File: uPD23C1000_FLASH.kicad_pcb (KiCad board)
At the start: 2 copper layers, 16.4 x 34.2 mm, 7 parts, among them J1 uPD23C1000, J2 Conn_1x2, J3 Conn_1x3, U1 GLS29EE010 (TSOP), U2 SST39SF010 (TSOP), U3 SST39SF010 / GLS29EE010 (PLCC)

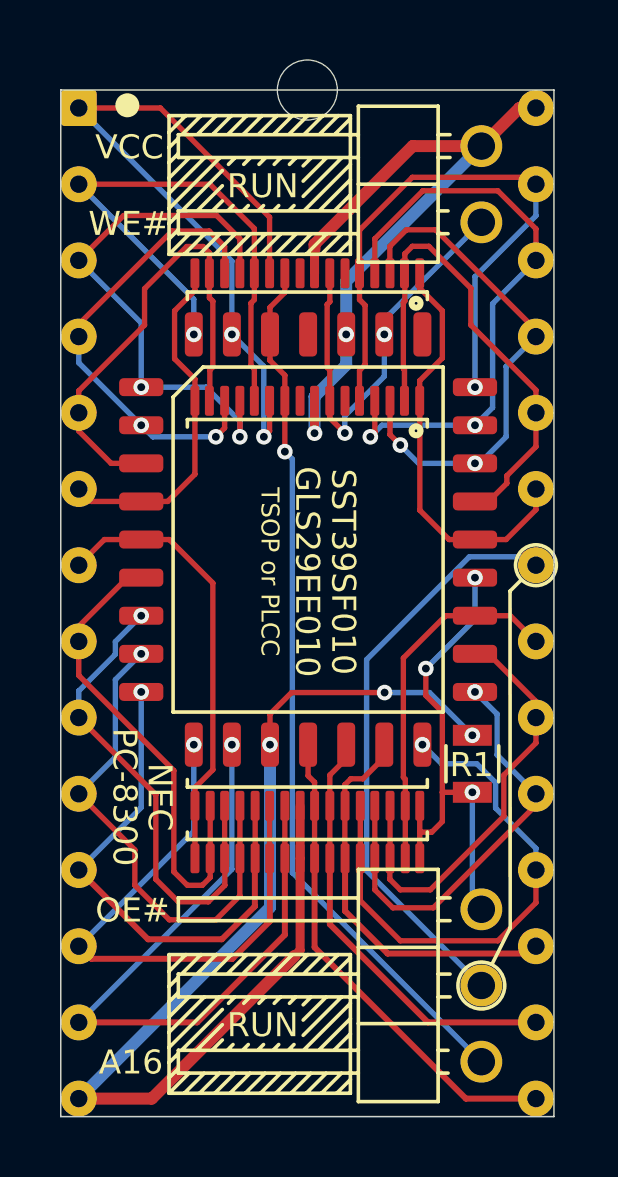
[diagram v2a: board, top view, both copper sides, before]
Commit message: Add FlexROM_100, FlexROM_102
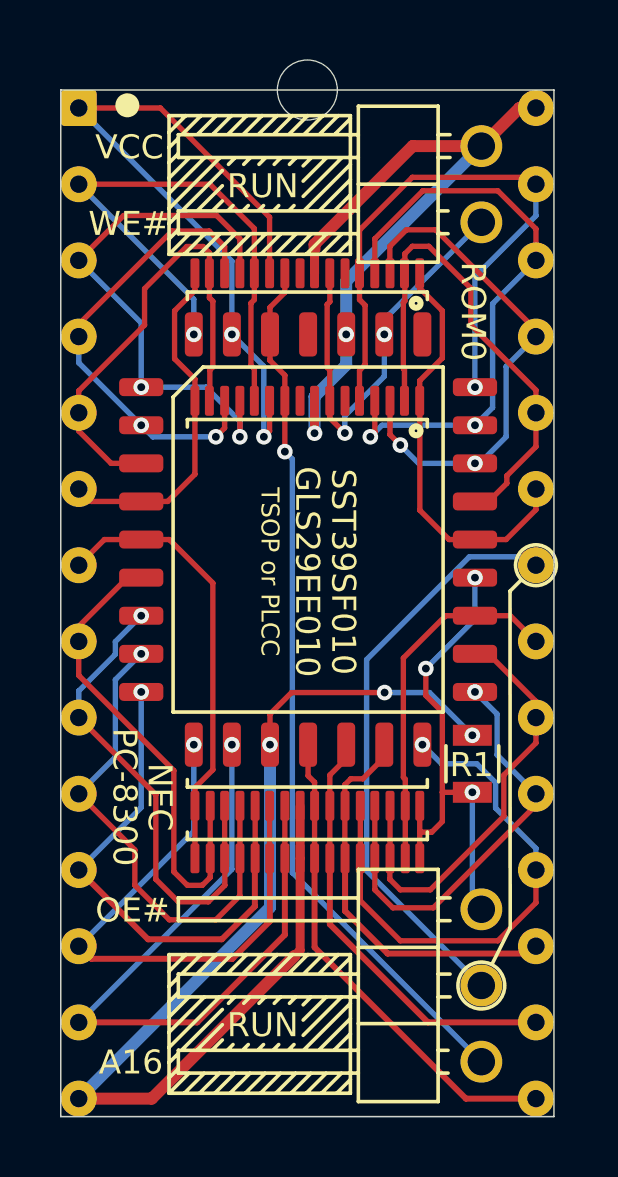
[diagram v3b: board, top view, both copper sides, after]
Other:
- board text added: "ROM0"
- board text added: "http://tandy.wiki/FlashROM_8300"
- board text removed: "tandy.wiki/FlashROM_8300"
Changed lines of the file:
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@@
   (general
     (thickness 1.6)
-    (drawings 141)
+    (drawings 142)
     (tracks 357)
     (zones 0)
@@
   (page A4)
   (layers
-    (0 F.Cu signal)
-    (31 B.Cu signal)
+    (0 F.Cu signal hide)
+    (31 B.Cu signal hide)
     (32 B.Adhes user hide)
     (33 F.Adhes user hide)
@@
     (37 F.SilkS user)
     (38 B.Mask user hide)
-    (39 F.Mask user hide)
+    (39 F.Mask user)
     (40 Dwgs.User user hide)
     (41 Cmts.User user hide)
@@
     )
   )
+  (gr_text ROM0 (at 155.5242 90.2716 -90) (layer F.SilkS)
+    (effects (font (size 0.8128 0.8128) (thickness 0.127)))
+  )
   (gr_text NEC (at 145.08 106.46 -90) (layer F.SilkS)
     (effects (font (size 0.8 0.8) (thickness 0.16)))
@@
     (effects (font (size 1 1) (thickness 0.15)) (justify mirror))
   )
-  (gr_text tandy.wiki/FlashROM_8300 (at 156 100 90) (layer B.SilkS)
+  (gr_text http://tandy.wiki/FlashROM_8300 (at 155.9814 98.7806 90) (layer B.SilkS)
     (effects (font (size 0.8 0.8) (thickness 0.1)) (justify mirror))
   )

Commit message: readme and silkscreen
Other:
- board text added: "39SF010"
- board text added: "Move A16 jumper to OE#"
- board text added: "Place board in programmer, 2 rows from the top"
- board text added: "Remove VCC/WE# jumper"
- board text removed: "GLS29EE010"
- board text removed: "Move A16 shunt to OE#"
- board text removed: "Place board in programmer 2 positions from top"
- board text removed: "Remove VCC/WE# shunt"
- board text removed: "SST39SF010"
- board text removed: "TSOP or PLCC"
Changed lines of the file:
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@@
   (general
     (thickness 1.6)
-    (drawings 142)
+    (drawings 140)
     (tracks 357)
     (zones 0)
@@
   (page A4)
   (layers
-    (0 F.Cu signal hide)
-    (31 B.Cu signal hide)
+    (0 F.Cu signal)
+    (31 B.Cu signal)
     (32 B.Adhes user hide)
     (33 F.Adhes user hide)
@@
     (37 F.SilkS user)
     (38 B.Mask user hide)
-    (39 F.Mask user)
+    (39 F.Mask user hide)
     (40 Dwgs.User user hide)
     (41 Cmts.User user hide)
@@
     (effects (font (size 0.8 0.8) (thickness 0.16)))
   )
-  (gr_text "TSOP or PLCC" (at 148.75 98.95 -90) (layer F.SilkS)
-    (effects (font (size 0.6 0.6) (thickness 0.08)))
-  )
   (gr_text "NEC PC-8300 System ROM" (at 145 100 90) (layer B.SilkS)
     (effects (font (size 1 1) (thickness 0.15)) (justify mirror))
@@
     (effects (font (size 0.6 0.6) (thickness 0.08)) (justify left mirror))
   )
-  (gr_text GLS29EE010 (at 150 98.95 -90) (layer F.SilkS)
-    (effects (font (size 0.8 0.8) (thickness 0.1)))
-  )
-  (gr_text SST39SF010 (at 151.2 98.95 -90) (layer F.SilkS)
+  (gr_text 39SF010 (at 150.025 97.875 -90) (layer F.SilkS)
     (effects (font (size 0.8 0.8) (thickness 0.1)))
   )
@@
     (effects (font (size 0.6 0.6) (thickness 0.08)) (justify left mirror))
   )
-  (gr_text "Remove VCC/WE# shunt" (at 148 84 90) (layer B.SilkS)
+  (gr_text "Remove VCC/WE# jumper" (at 148 84 90) (layer B.SilkS)
     (effects (font (size 0.6 0.6) (thickness 0.08)) (justify left mirror))
   )
@@
     (effects (font (size 0.6 0.6) (thickness 0.08)) (justify left mirror))
   )
-  (gr_text "Place board in programmer 2 positions from top" (at 150 84 90) (layer B.SilkS)
+  (gr_text "Place board in programmer, 2 rows from the top" (at 150 84 90) (layer B.SilkS)
     (effects (font (size 0.6 0.6) (thickness 0.08)) (justify left mirror))
   )
@@
     (effects (font (size 0.6 0.6) (thickness 0.08)) (justify left mirror))
   )
-  (gr_text "Move A16 shunt to OE#" (at 149 84 90) (layer B.SilkS)
+  (gr_text "Move A16 jumper to OE#" (at 149 84 90) (layer B.SilkS)
     (effects (font (size 0.6 0.6) (thickness 0.08)) (justify left mirror))
   )
